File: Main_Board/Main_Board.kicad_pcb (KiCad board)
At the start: 4 copper layers, 80.5 x 75.6 mm, 68 parts, among them IC1 AZ1085CD-3.3TRG1, J1 PJ-037A, U1 STM32L152ZCTx, U2 LM386, Y1 ABM10W-16.0000MHZ-4-B1U-T3

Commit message: update
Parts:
- moved Speaker-1 0.19 mm to (128.9, 27.9)
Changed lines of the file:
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@@
     (tags "Integrated Circuit")
     (attr smd)
-    (fp_text reference U2 (at -1.99136 2.60604) (layer F.SilkS)
-      (effects (font (size 1.27 1.27) (thickness 0.254)))
-    )
-    (fp_text value LM386 (at -2.0574 2.413) (layer F.SilkS) hide
+    (fp_text reference U2 (at -1.5748 5.0292) (layer F.SilkS)
+      (effects (font (size 1.27 1.27) (thickness 0.254)))
+    )
+    (fp_text value LM386 (at -1.4732 4.9784) (layer F.SilkS) hide
       (effects (font (size 1.27 1.27) (thickness 0.254)))
     )
@@
   )
   (module MountingHole:MountingHole_2.5mm_Pad (layer F.Cu)
-    (at 128.78308 27.75458)
+    (at 128.8796 27.9146)
     (descr "Mounting Hole 2.5mm")
     (tags "mounting hole 2.5mm")
@@
     (pad 3 smd rect (at 2.3 5.35 180) (size 1.5 2.5) (layers F.Cu F.Paste F.Mask)
       (net 17 +5V))
+    (model C:/Users/agf20/Downloads/ZLDO1117K33TC-pcb-part-libraries/SamacSys_Parts.3dshapes/IRLR8256PBF.stp
+      (offset (xyz -0 -1.524 0))
+      (scale (xyz 1 1 1))
+      (rotate (xyz 0 0 0))
+    )
   )
   (module Connector_PinHeader_2.54mm:PinHeader_1x09_P2.54mm_Vertical (layer F.Cu)

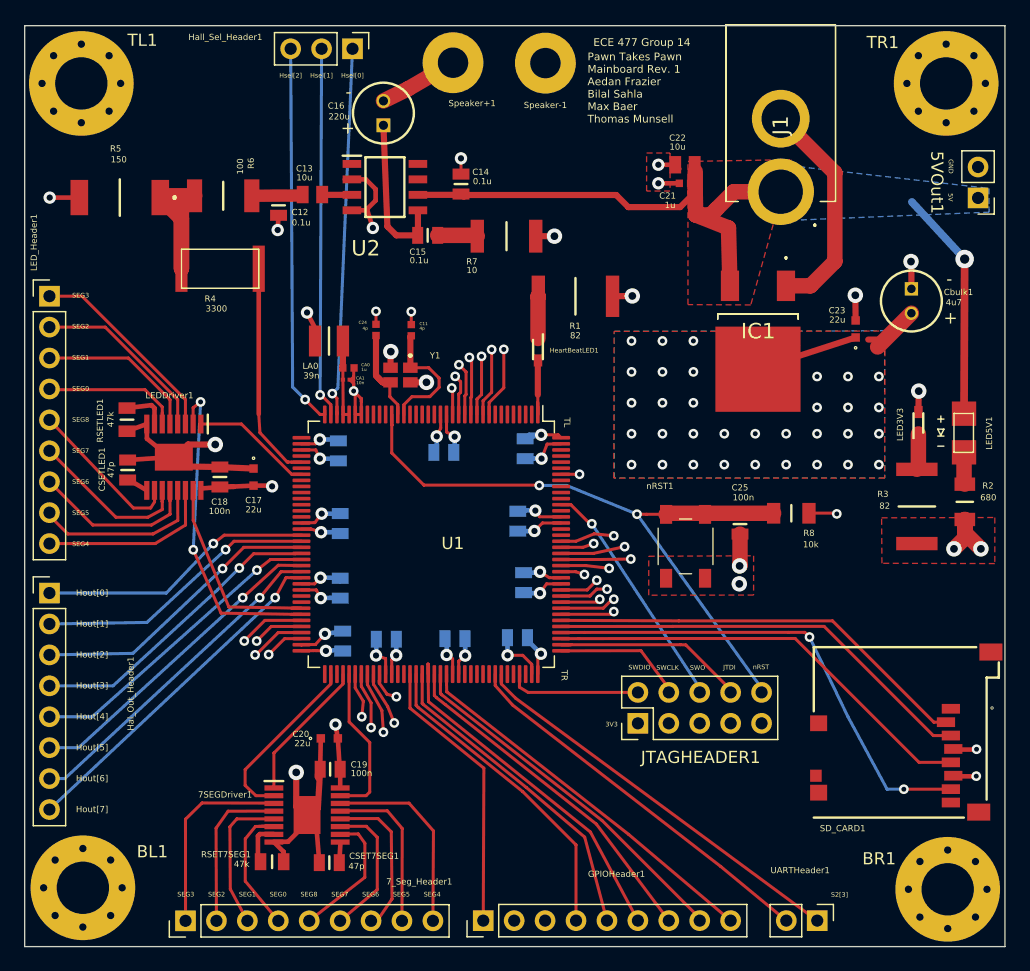
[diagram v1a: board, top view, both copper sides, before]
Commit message: edited main board headers for buttons, daughterboard power
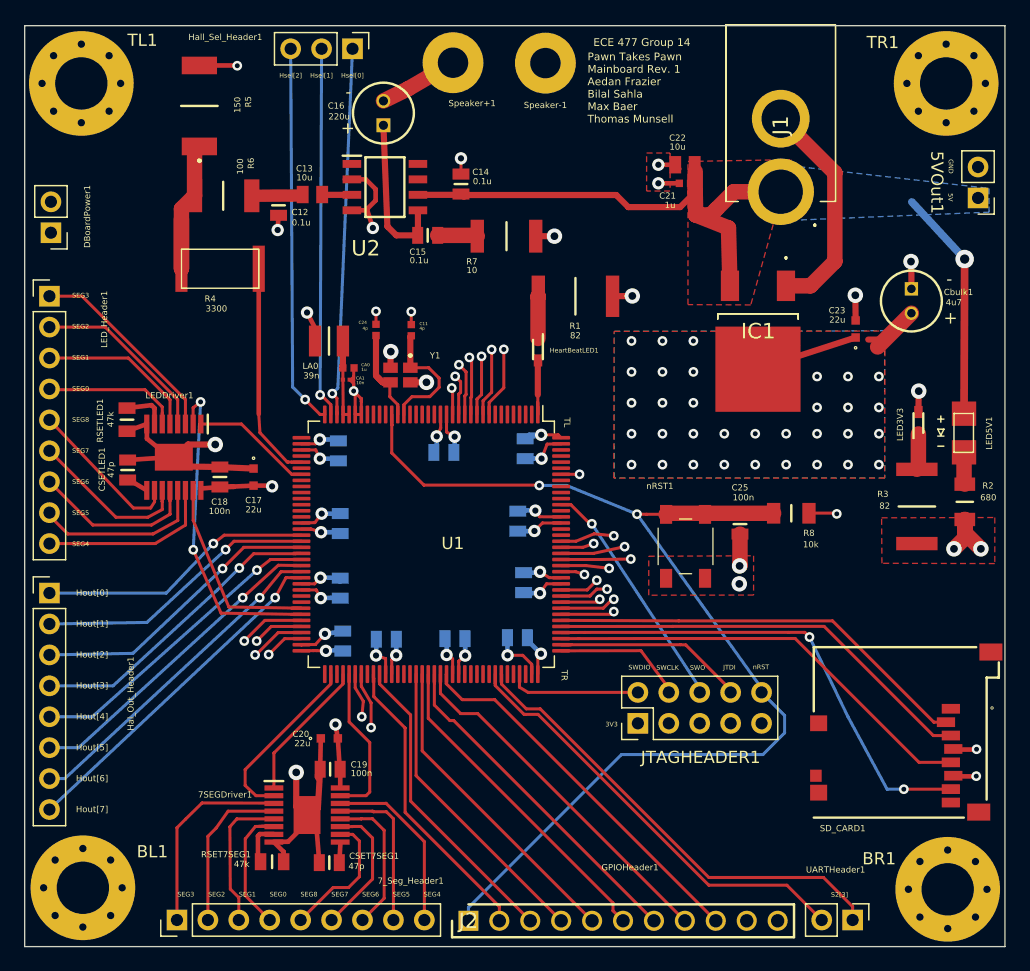
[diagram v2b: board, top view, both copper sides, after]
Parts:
- removed GPIOHeader1: Conn_01x09, Connector_PinHeader_2.54mm:PinHeader_1x09_P2.54mm_Vertical
- added DBoardPower1: Conn_01x02_Male, Main_Board:PinHeader_1x02_P2.54mm_Vertical, F.Cu at (88.3, 41.8)
- added J2: 77311-862-11LF, Main_Board:HDRV11W62P0X254_1X11_2794X240X853P, F.Cu at (122.6, 98.4)
- moved R5 9.97 mm to (100.5, 31.4), turned to 90 degrees
- moved UARTHeader1 2.91 mm to (154.1, 98.3)
- moved 7_Seg_Header1 0.71 mm to (98.6, 98.3)
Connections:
- U1 pad 81: Net-(U1-Pad81) -> B1
- U1 pad 82: Net-(U1-Pad82) -> B2
- U1 pad 87: Reset_Line -> Net-(U1-Pad87)
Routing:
- net nRST: track 64.3 -> 101.4 mm
- net B2: track 0.00 -> 25.4 mm
- net B1: track 0.00 -> 24.5 mm
- net Reset_Line: track 23.1 -> 0.00 mm
- net USART1_RX: track 33.2 -> 38.3 mm
- net Net-(U1-Pad80): track 5.09 -> 0.00 mm, vias 1 -> 0
- net Net-(U1-Pad81): track 4.46 -> 0.00 mm, vias 1 -> 0
- net USART1_TX: track 31.7 -> 35.8 mm
- net Net-(U1-Pad82): track 2.66 -> 0.00 mm, vias 1 -> 0
- net /SEG4_7SEG: track 17.1 -> 14.7 mm
- net S1[3]: track 29.3 -> 26.9 mm
- net /SEG2_7SEG: track 13.9 -> 12.6 mm
- net /SEG1_7SEG: track 13.1 -> 11.9 mm
- net Net-(R4-Pad1): track 15.9 -> 14.8 mm
- net S1[1]: track 26.2 -> 25.2 mm
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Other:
- board text added: "GPIOHeader1"

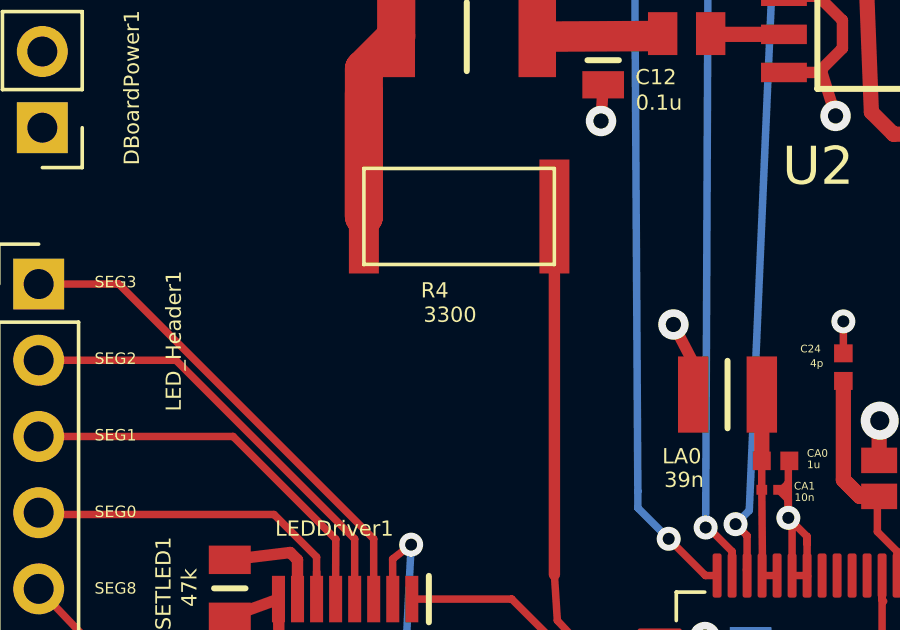
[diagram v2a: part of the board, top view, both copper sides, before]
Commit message: changed audio resistor value, same package
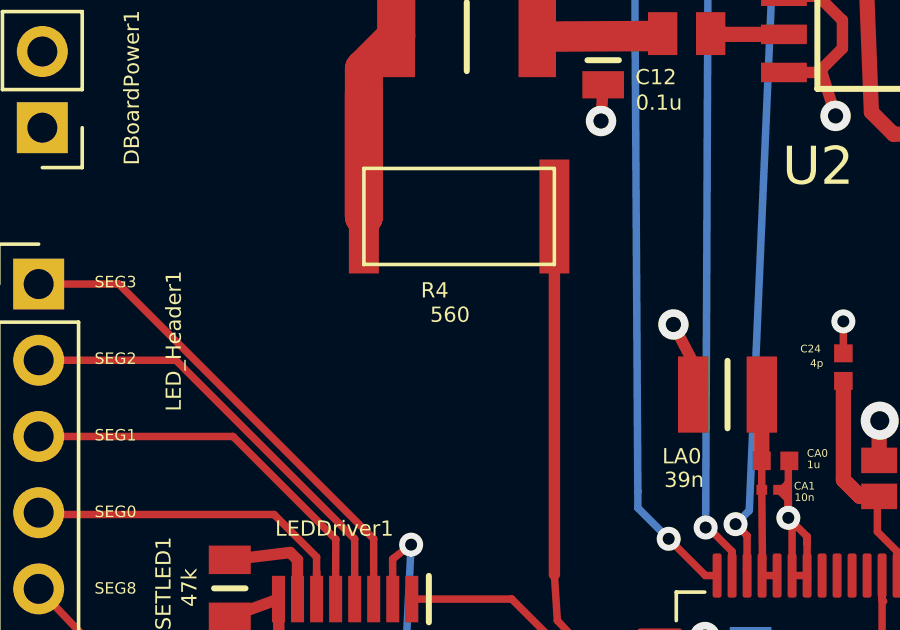
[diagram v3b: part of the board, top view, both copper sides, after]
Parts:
- R4: value 3300 -> 560

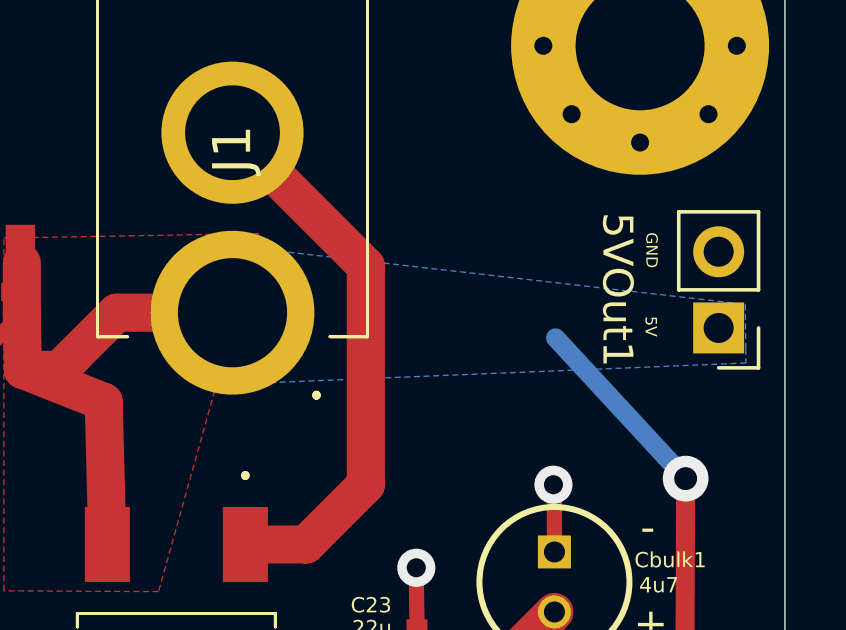
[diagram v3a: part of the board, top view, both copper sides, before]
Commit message: changed 5V trace
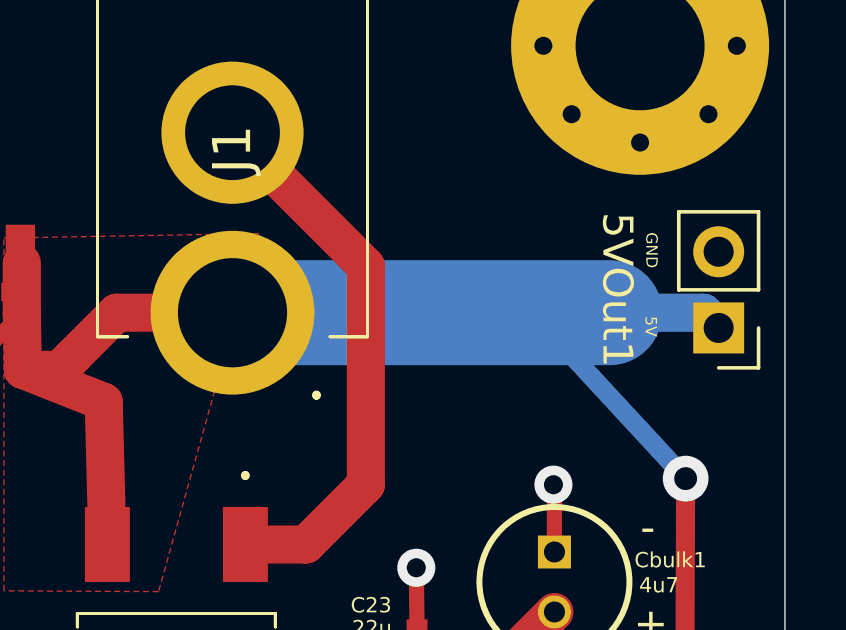
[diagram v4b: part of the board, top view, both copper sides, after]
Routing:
- net +5V: track 62.2 -> 78.6 mm
- removed copper zone on B.Cu, net +5V
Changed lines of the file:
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@@
     (thickness 1.6)
     (drawings 55)
-    (tracks 799)
+    (tracks 802)
     (zones 0)
     (modules 69)
@@
   )
   (setup
-    (last_trace_width 0.25)
+    (last_trace_width 1.27)
     (user_trace_width 0.381)
     (user_trace_width 0.508)
     (user_trace_width 1.27)
+    (user_trace_width 3.5)
     (trace_clearance 0.2)
     (zone_clearance 0.508)
@@
   (segment (start 143.9164 41.4528) (end 144.038699 46.207199) (width 1.27) (layer F.Cu) (net 17))
   (segment (start 141.224 40.386) (end 143.9164 41.4528) (width 1.27) (layer F.Cu) (net 17))
+  (segment (start 148.209 38.481) (end 160.782 38.481) (width 3.5) (layer B.Cu) (net 17))
+  (segment (start 163.9062 38.481) (end 164.4142 38.989) (width 1.27) (layer B.Cu) (net 17))
+  (segment (start 160.782 38.481) (end 163.9062 38.481) (width 1.27) (layer B.Cu) (net 17))
   (via (at 134.49808 66.74358) (size 0.8) (drill 0.4) (layers F.Cu B.Cu) (net 28))
   (segment (start 131.390302 67.187) (end 130.1695 67.187) (width 0.25) (layer F.Cu) (net 28))
@@
       )
     )
-  )
-  (zone (net 17) (net_name +5V) (layer B.Cu) (hatch edge 0.508)
-    (connect_pads yes (clearance 0.508))
-    (min_thickness 0.254)
-    (fill yes (arc_segments 32) (thermal_gap 0.508) (thermal_bridge_width 0.508))
-    (polygon
-      (pts
-        (xy 165.3159 39.6875) (xy 165.3286 40.1574) (xy 148.082 40.8686) (xy 148.1582 36.2458) (xy 165.3032 38.2016)
-      )
-    )

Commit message: gerbers
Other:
- rule pad_to_mask_clearance: 0.051 -> 0

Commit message: ESD and Pullups
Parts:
- added R10: 50k, RESC1005X40N, F.Cu at (125.1, 93.3)
- added R11: 50k, RESC1005X40N, F.Cu at (127.6, 93.3)
- added R12: 50k, RESC1005X40N, F.Cu at (130.2, 93.3)
- added R13: 50k, RESC1005X40N, F.Cu at (132.7, 93.3)
- added R14: 50k, RESC1005X40N, F.Cu at (135.3, 93.3)
- added R15: 50k, RESC1005X40N, F.Cu at (137.8, 93.3)
- added R16: 50k, RESC1005X40N, F.Cu at (140.3, 93.3)
- added R17: 50k, RESC1005X40N, F.Cu at (142.9, 93.3)
- added R18: 10k, SamacSys_Parts:RESC3116X70N, F.Cu at (157.0, 73.7)
- added R19: 10k, SamacSys_Parts:RESC3116X70N, B.Cu at (162.2, 76.3)
- added R20: 10k, SamacSys_Parts:RESC3116X70N, B.Cu at (154.2, 90.1)
- added R9: 50k, RESC1005X40N, F.Cu at (122.6, 93.3)
- UARTHeader1: footprint Connector_PinHeader_2.54mm:PinHeader_1x02_P2.54mm_Vertical -> Main_Board:PinHeader_1x02_P2.54mm_Vertical
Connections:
- J2 pad 1: nRST -> Net-(J2-Pad1)
- J2 pad 2: B1 -> Net-(J2-Pad2)
- J2 pad 3: B2 -> Net-(J2-Pad3)
- J2 pad 4: S1[1] -> Net-(J2-Pad4)
- J2 pad 5: S1[2] -> Net-(J2-Pad5)
- J2 pad 6: S1[3] -> Net-(J2-Pad6)
- J2 pad 7: S2[1] -> Net-(J2-Pad7)
- J2 pad 8: S2[2] -> Net-(J2-Pad8)
- J2 pad 9: S2[3] -> Net-(J2-Pad9)
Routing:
- net Net-(R20-Pad1): track 0.00 -> 8.06 mm, vias 0 -> 1
- net S1[1]: track 25.2 -> 19.6 mm
- net B2: track 25.4 -> 20.1 mm
- net B1: track 24.5 -> 19.3 mm
- net +3V3: track 90.2 -> 94.9 mm, vias 50 -> 53
- net Net-(J2-Pad7): track 0.00 -> 4.55 mm
- net Net-(J2-Pad9): track 0.00 -> 4.47 mm
- net Net-(J2-Pad8): track 0.00 -> 4.47 mm
- net Net-(J2-Pad6): track 0.00 -> 4.47 mm
- net Net-(J2-Pad5): track 0.00 -> 4.47 mm
- net Net-(J2-Pad4): track 0.00 -> 4.47 mm
- net Net-(J2-Pad3): track 0.00 -> 4.47 mm
- net Net-(J2-Pad2): track 0.00 -> 4.47 mm
- net Net-(J2-Pad1): track 0.00 -> 4.47 mm
- net S1[2]: track 26.0 -> 22.5 mm
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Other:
- board text added: "B1"
- board text added: "B2"
- board text added: "RX"
- board text added: "S1[1]"
- board text added: "S1[2]"
- board text added: "S1[3]"
- board text added: "S2[1]"
- board text added: "S2[2]"
- board text added: "TX"
- board text removed: "GPIOHeader1"
